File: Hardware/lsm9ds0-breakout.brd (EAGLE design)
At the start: 33 x 15.2 mm, 21 parts, among them U1 LSM9DS0

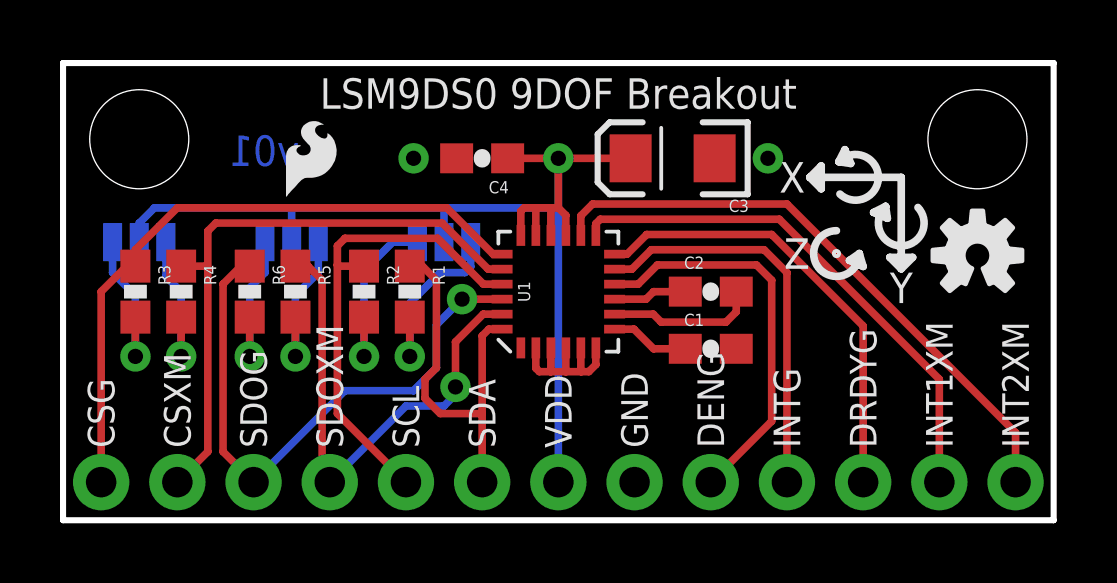
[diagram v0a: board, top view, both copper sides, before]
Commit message: Fixed some silk. Moved some vias.
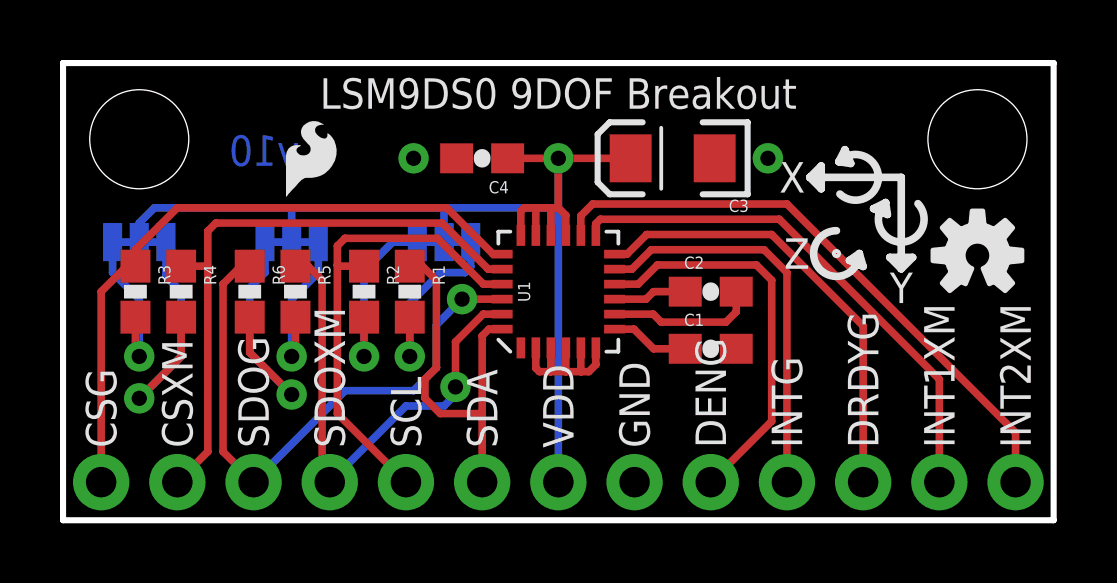
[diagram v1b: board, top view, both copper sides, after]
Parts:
- moved LOGO2 4.02 mm to (32.1, 7.24)
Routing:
- net N$5: track 5.33 -> 9.28 mm
- net N$13: track 5.33 -> 9.03 mm
- net N$10: track 0.00 -> 0.64 mm
- net N$9: track 0.00 -> 0.64 mm
- net N$8: track 0.00 -> 0.63 mm
- net N$15: track 0.00 -> 0.63 mm
- net N$14: track 0.00 -> 0.63 mm
- net N$11: track 0.00 -> 0.63 mm
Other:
- board text added: "2"
- board text added: "G 6A 6B"
- board text added: "I C Address"
- board text added: "SDOX/G"
- board text added: "XM 1E 1D"
- board text added: "v10"
- board text removed: "1E 1D"
- board text removed: "Addr"
- board text removed: "SA0"
- board text removed: "v01"

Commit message: Adding fiducials
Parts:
- added FID1, FID2: FIDUCIALUFIDUCIAL, SparkFun-Aesthetics:MICRO-FIDUCIAL
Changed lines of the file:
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@@
 <element name="LOGO3" library="SparkFun-Aesthetics" package="SFE_LOGO_FLAME_.1" value="SFE_LOGO_FLAME.1_INCH" x="7.112" y="10.414"/>
 <element name="LOGO2" library="SparkFun-Aesthetics" package="SFE_LOGO_FLAME_.1" value="SFE_LOGO_FLAME.1_INCH" x="32.131" y="7.239" rot="MR0"/>
+<element name="FID1" library="SparkFun-Aesthetics" package="MICRO-FIDUCIAL" value="FIDUCIALUFIDUCIAL" x="30.48" y="5.334"/>
+<element name="FID2" library="SparkFun-Aesthetics" package="MICRO-FIDUCIAL" value="FIDUCIALUFIDUCIAL" x="0.762" y="14.478"/>
 </elements>
 <signals>
